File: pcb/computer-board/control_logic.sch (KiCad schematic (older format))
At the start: 13 parts, among them U14 XC95144XL-10TQ100C, U15 74LVC16374ADGG,112

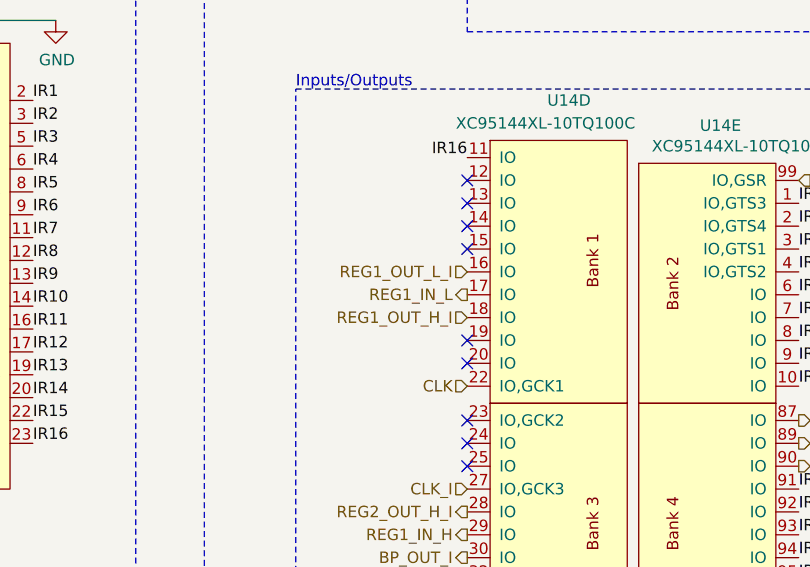
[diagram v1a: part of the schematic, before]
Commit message: Remove and change connectors for a mezzanine one
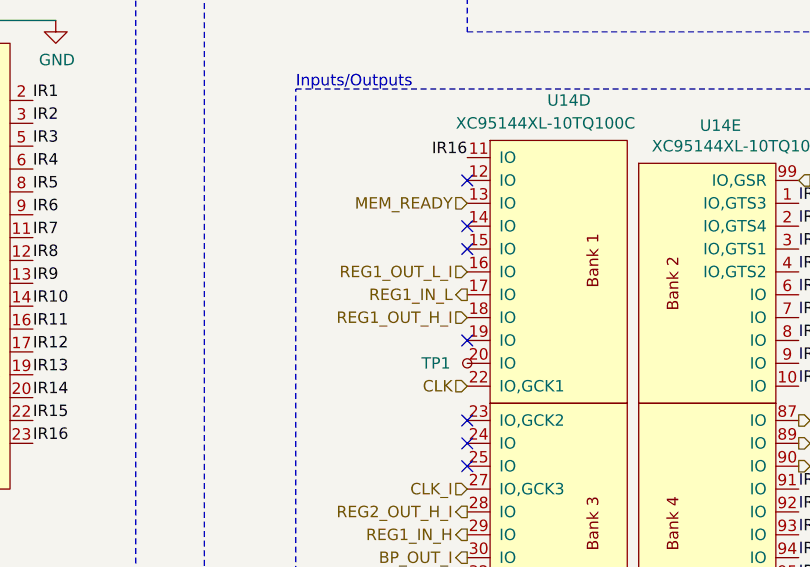
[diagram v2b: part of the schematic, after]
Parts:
- added TP1: TestPoint_Small, TestPoint:TestPoint_Pad_D1.0mm, symbol Connector:TestPoint_Small
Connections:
- net MEM_READY: now reaches U14.13 (IO)
- net at U14.20 (IO): now also TP1.1
- no-connect marks 21 -> 19
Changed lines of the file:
@@
-$Comp
-L XC9500XL:XC95144XL-10TQ100C U14
-U 4 1 5FA7DC14
-P 4450 2400
-F 0 "U14" H 4200 2400 50  0000 R CNN
-F 1 "XC95144XL-10TQ100C" H 4600 2300 50  0000 R CNN
-F 2 "Package_QFP:TQFP-100_14x14mm_P0.5mm" H 4450 2400 50  0001 C CNN
-F 3 "" H 4450 2400 50  0001 C CNN
-	4    4450 2400
-	-1   0    0    -1
-$EndComp
 $Comp
 L XC9500XL:XC95144XL-10TQ100C U14
@@
 REG3_IN_L
 NoConn ~ 4350 2750
-NoConn ~ 4350 2850
 NoConn ~ 4350 2950
 NoConn ~ 4350 3050
 NoConn ~ 4350 3450
-NoConn ~ 4350 3550
 NoConn ~ 4350 3800
 NoConn ~ 4350 3900
@@
 NoConn ~ 6900 4400
 NoConn ~ 6900 4500
+$Comp
+L Connector:TestPoint_Small TP1
+U 1 1 5FC4803C
+P 4350 3550
+F 0 "TP1" H 4150 3550 50  0000 L CNN
+F 1 "TestPoint_Small" H 4398 3505 50  0001 L CNN
+F 2 "TestPoint:TestPoint_Pad_D1.0mm" H 4550 3550 50  0001 C CNN
+F 3 "~" H 4550 3550 50  0001 C CNN
+	1    4350 3550
+	1    0    0    -1
+$EndComp
+$Comp
+L XC9500XL:XC95144XL-10TQ100C U14
+U 4 1 5FA7DC14
+P 4450 2400
+F 0 "U14" H 4200 2400 50  0000 R CNN
+F 1 "XC95144XL-10TQ100C" H 4600 2300 50  0000 R CNN
+F 2 "Package_QFP:TQFP-100_14x14mm_P0.5mm" H 4450 2400 50  0001 C CNN
+F 3 "" H 4450 2400 50  0001 C CNN
+	4    4450 2400
+	-1   0    0    -1
+$EndComp
+Text HLabel 4350 2850 0    50   Input ~ 0
+MEM_READY
 $EndSCHEMATC
